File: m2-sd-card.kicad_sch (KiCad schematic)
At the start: 16 parts, among them J101 M.2_Key_E, J102 Conn_01x02, J103 Conn_02x03_Counter_Clockwise, J104 Conn_02x03_Counter_Clockwise, J105 Conn_01x01, J106 Conn_01x03, J107 Conn_01x02, J108 USB_B_Micro, J109 Micro_SD, U101 SN74LV1T34DBV

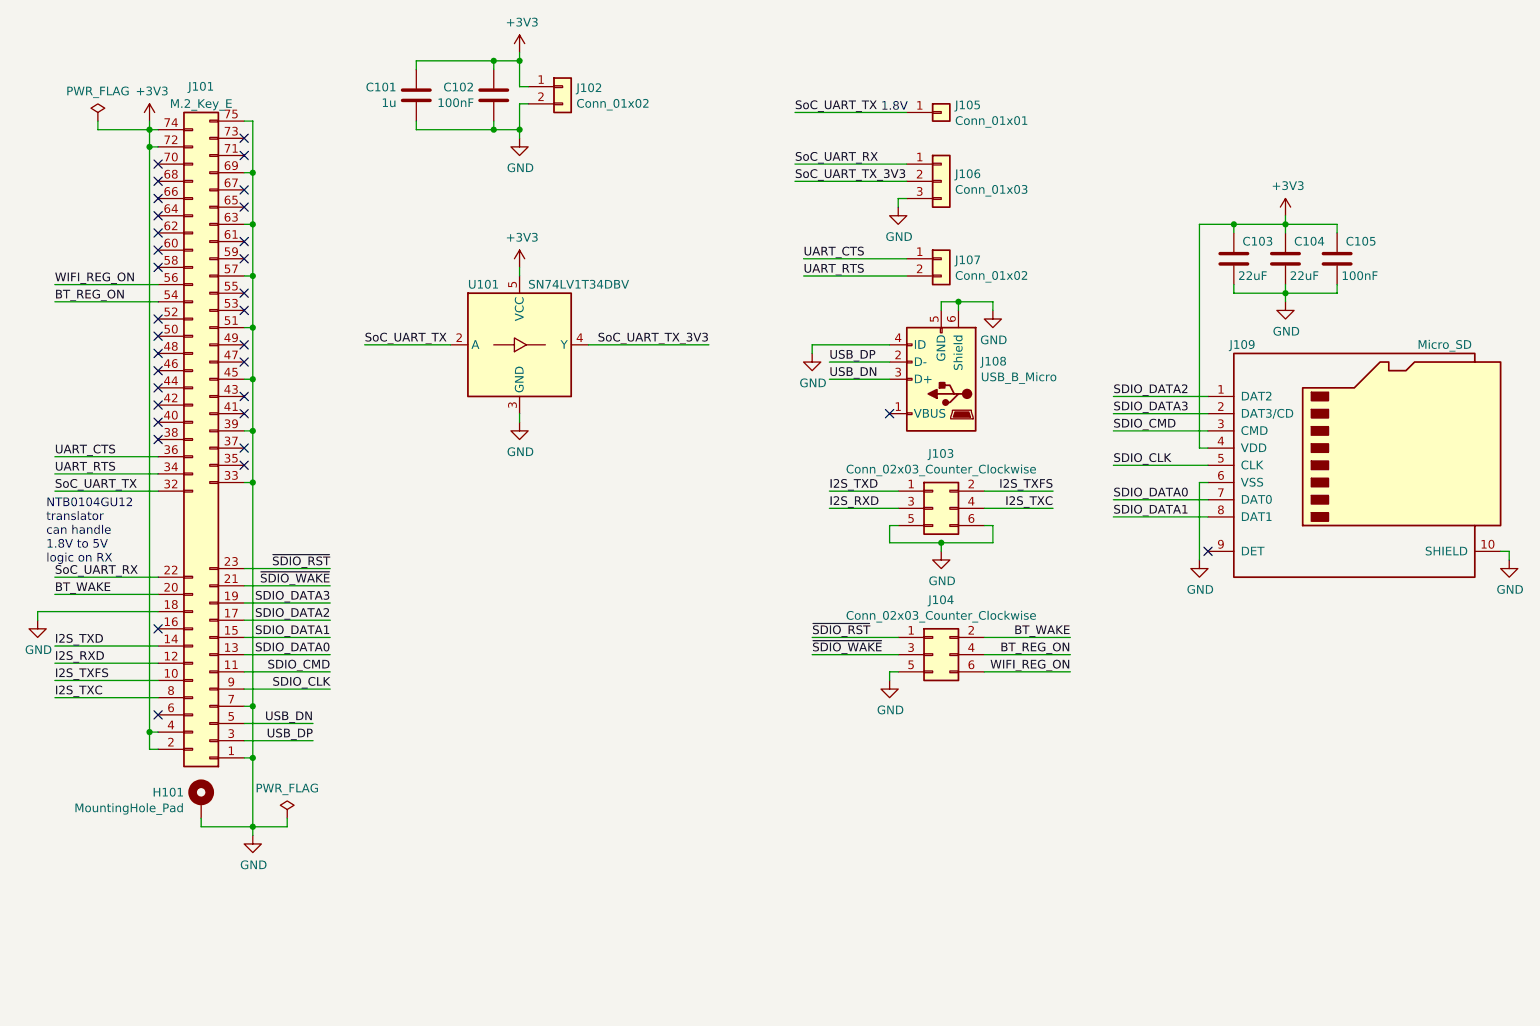
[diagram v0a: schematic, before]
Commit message: Update the schematic to use the NVT4857UK SD 3.0-compliant bidirectional level translator
Use Hirose DM3AT-SF-PEJM5 for the MicroSD card slot/connector (using
KiCad's built-in library, with the footprint backed up in the project
library).

Add a AP2120N-1.8 1.8V LDO to supply NVT4857UK's VCCA.

Create the NVT4857UK schematic symbol and footprint.

Create the AP2120N-18 schematic symbol.

Connect everything in the schematic, annotate all parts, and make sure
ERC passes.

Capacitors' and resistors' part numbers still need to be selected and
their attributes updated accordingly. Then the netlist can be imported
into the layout and the BOM exported.

At least 4mil trace width/space is likely needed due to the WLCSP-20
BGA package.
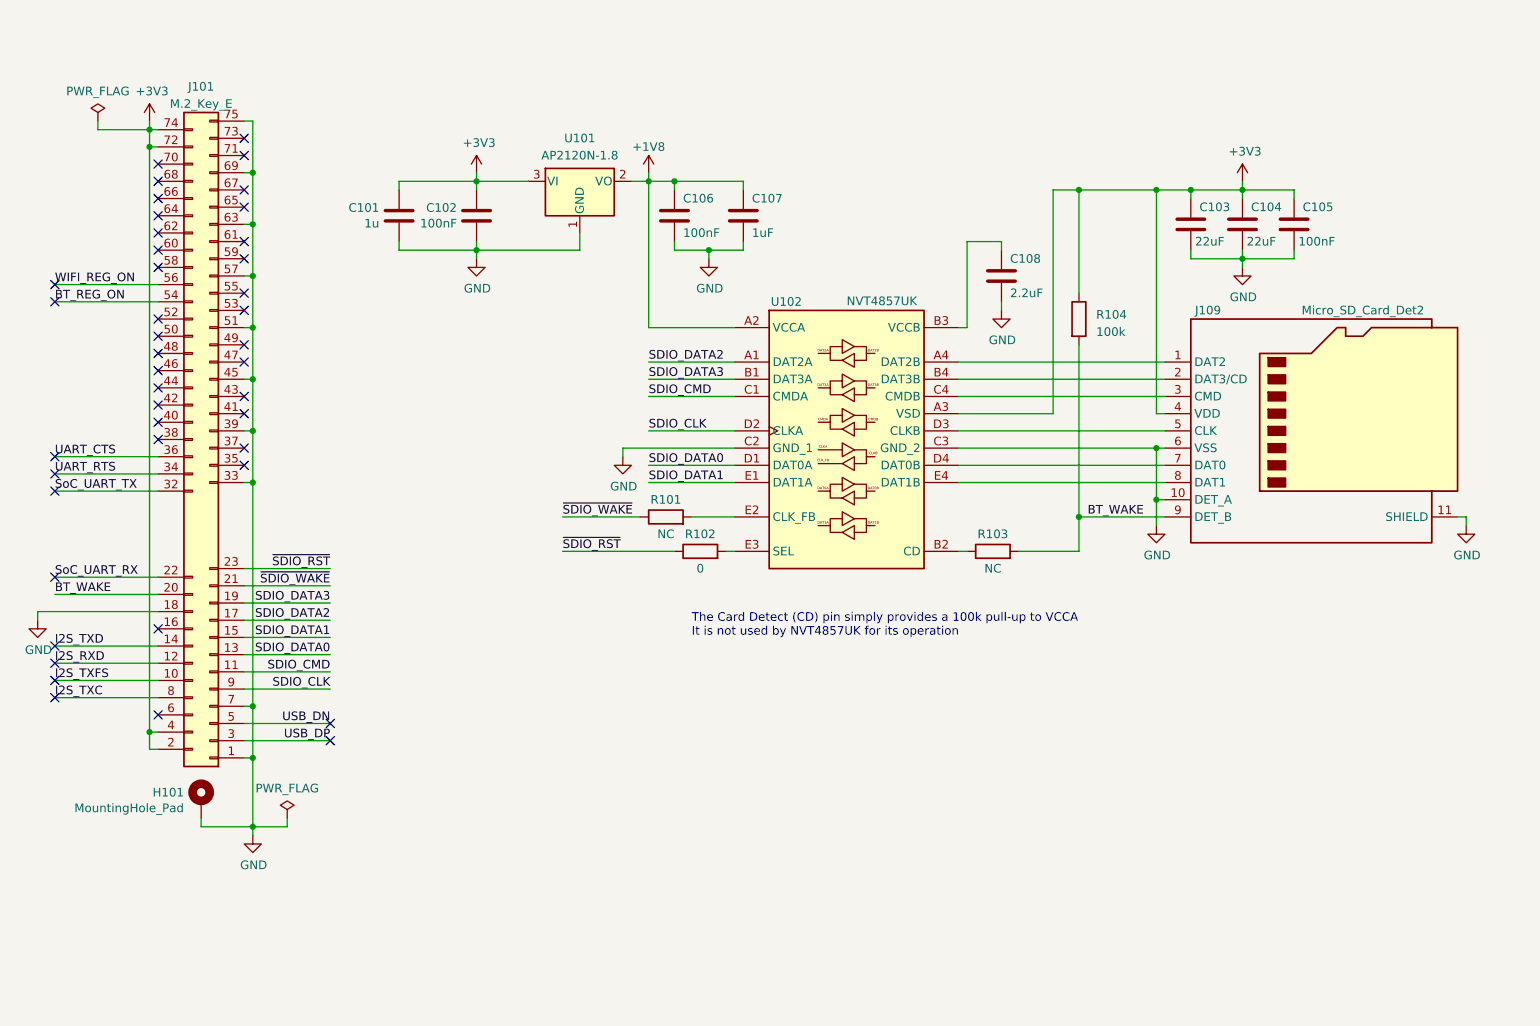
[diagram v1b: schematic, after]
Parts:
- removed J102: Conn_01x02, Connector_PinHeader_2.54mm:PinHeader_1x02_P2.54mm_Vertical, symbol Connector_Generic:Conn_01x02
- removed J103, J104: Conn_02x03_Counter_Clockwise, Connector_PinHeader_1.27mm:PinHeader_2x03_P1.27mm_Vertical_SMD, symbol Connector_Generic:Conn_02x03_Odd_Even
- removed J105: Conn_01x01, Connector_PinHeader_2.54mm:PinHeader_1x01_P2.54mm_Vertical, symbol Connector_Generic:Conn_01x01
- removed J106: Conn_01x03, Connector_PinHeader_2.54mm:PinHeader_1x03_P2.54mm_Vertical, symbol Connector_Generic:Conn_01x03
- removed J107: Conn_01x02, Connector_PinHeader_1.27mm:PinHeader_1x02_P1.27mm_Vertical_SMD_Pin1Right, symbol Connector_Generic:Conn_01x02
- removed J108: USB_B_Micro, Connector_USB:USB_Micro-B_Wuerth_614105150721_Vertical, symbol Connector:USB_OTG
- removed J109: Micro_SD, m2-sd-card:ALPS_SCHA4B0419, symbol m2-sd-card:Micro_SD_Card_Det_ALPS_SCHA
- removed U101: SN74LV1T34DBV, Package_TO_SOT_SMD:SOT-23-5_HandSoldering, symbol m2-sd-card:SN74LV1T34DBV
- added C106: 100nF, Capacitor_SMD:C_0402_1005Metric, symbol Device:C
- added C107: 1uF, Capacitor_SMD:C_0402_1005Metric, symbol Device:C
- added C108: 2.2uF, Capacitor_SMD:C_0402_1005Metric, symbol Device:C
- added J109: Micro_SD_Card_Det2, Connector_Card:microSD_HC_Hirose_DM3AT-SF-PEJM5, symbol Connector:Micro_SD_Card_Det2
- added R101, R103: NC, Resistor_SMD:R_0402_1005Metric, symbol Device:R
- added R102: 0, Resistor_SMD:R_0402_1005Metric, symbol Device:R
- added R104: 100k, Resistor_SMD:R_0402_1005Metric, symbol Device:R
- added U101: AP2120N-1.8, Package_TO_SOT_SMD:SOT-23, symbol m2-sd-card:AP2120N-1.8
- added U102: NVT4857UK, m2-sd-card:NVT4857UK, symbol m2-sd-card:NVT4857UK
- C101, C102, C103, C104, C105: footprint Capacitor_SMD:C_0603_1608Metric_Pad1.05x0.95mm_HandSolder -> Capacitor_SMD:C_0402_1005Metric
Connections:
- net +3V3: now also J109.4 (VDD), R104.1, U101.3 (VI), U102.A3 (VSD)
- net BT_WAKE: now also J109.9 (DET_B), R103.2, R104.2
- net GND: now also C106.2, C107.2, C108.2, J109.10 (DET_A), J109.11 (SHIELD), J109.6 (VSS), U101.1 (GND), U102.C2 (GND_1), U102.C3 (GND_2)
- net SDIO_CLK: now also U102.D2 (CLKA)
- net SDIO_CMD: now also U102.C1 (CMDA)
- net SDIO_DATA0: now also U102.D1 (DAT0A)
- net SDIO_DATA1: now also U102.E1 (DAT1A)
- net SDIO_DATA2: now also U102.A1 (DAT2A)
- net SDIO_DATA3: now also U102.B1 (DAT3A)
- net ~{SDIO_RST}: now also R102.1
- net ~{SDIO_WAKE}: now also R101.1
- new net: R102.2, U102.E3 (SEL)
- new net: C108.1, U102.B3 (VCCB)
- new net: J109.1 (DAT2), U102.A4 (DAT2B)
- new net: R103.1, U102.B2 (CD)
- new net: J109.2 (DAT3/CD), U102.B4 (DAT3B)
- new net: J109.3 (CMD), U102.C4 (CMDB)
- new net: J109.5 (CLK), U102.D3 (CLKB)
- new net: J109.7 (DAT0), U102.D4 (DAT0B)
- new net: R101.2, U102.E2 (CLK_FB)
- new net: J109.8 (DAT1), U102.E4 (DAT1B)
- new net +1V8: C106.1, C107.1, U101.2 (VO), U102.A2 (VCCA)
- no-connect marks 33 -> 43
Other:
- note added: "The Card Detect (CD) pin simply provides a 100k pull-up to VCCA It is not used by NVT4857UK for its operation"
- note removed: "1.8V"
- note removed: "NTB0104GU12 translator can handle 1.8V to 5V logic on RX"
- moved on the sheet: C101, C102, C103, C104, C105

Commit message: Fill out the remaining attributes for the passives and export the BOM and schematic as a PDF
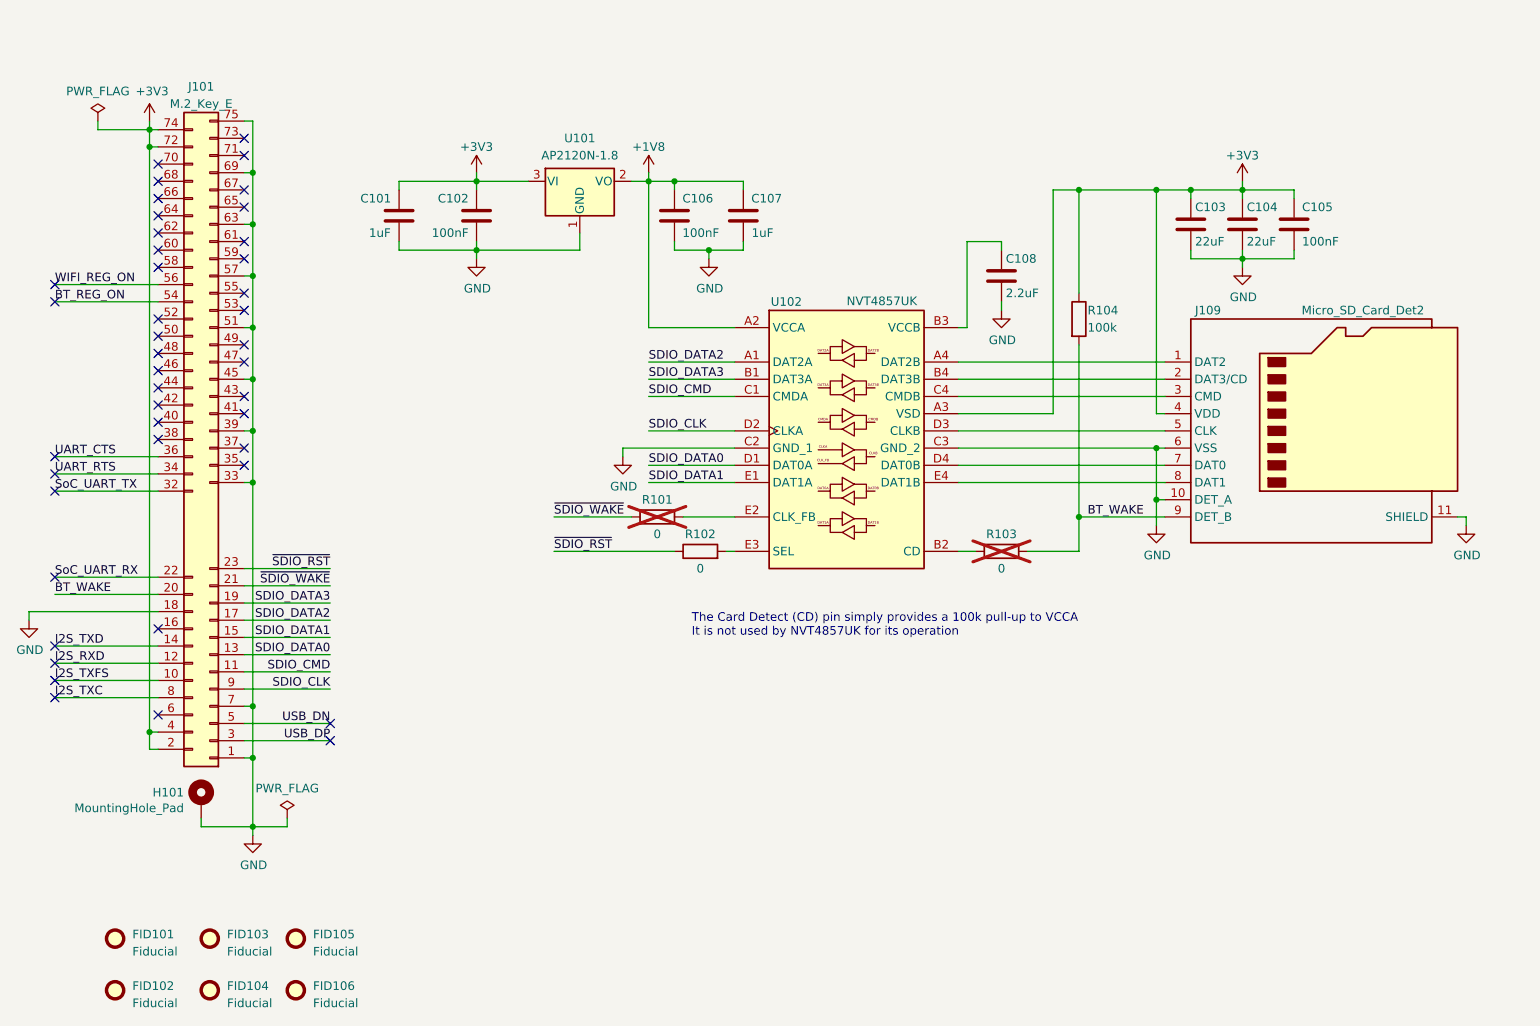
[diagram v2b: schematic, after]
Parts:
- added FID101, FID102, FID103, FID104, FID105, FID106: Fiducial, Fiducial:Fiducial_0.5mm_Mask1mm, symbol Mechanical:Fiducial
- C101: value 1u -> 1uF; Distrib Link (none) -> https://www.mouser.com/ProductDetail/Samsung-Electro-Mechan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; Distrib PN (none) -> 187-CL05A105KO5NNNC; MFG Name (none) -> Samsung; MFG Part Num (none) -> CL05A105KO5NNNC; Others (none) -> https://www.mouser.com/c/passive-components/capacitors/mlcc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; Tolerance (none) -> 10%
- C102, C105, C106: Distrib Link (none) -> https://www.mouser.com/ProductDetail/Samsung-Electro-Mechan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; Distrib PN (none) -> 187-CL05A104KA5NNNC; MFG Name (none) -> Samsung; MFG Part Num (none) -> CL05A104KA5NNNC; Others (none) -> https://www.mouser.com/c/passive-components/capacitors/mlcc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; Tolerance (none) -> 10%
- C103, C104: Distrib Link (none) -> https://www.mouser.com/ProductDetail/KYOCERA-AVX/CM05X5R226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; Distrib PN (none) -> 346-CM05X5R226M6AH80; MFG Name (none) -> KYOCERA AVX; MFG Part Num (none) -> CM05X5R226M06AH080; Others (none) -> https://www.digikey.com/en/products/detail/kyocera-avx/CM05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; Tolerance (none) -> 20%
- C107: Distrib Link (none) -> https://www.mouser.com/ProductDetail/Samsung-Electro-Mechan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; Distrib PN (none) -> 187-CL05A105KO5NNNC; MFG Name (none) -> Samsung; MFG Part Num (none) -> CL05A105KO5NNNC; Others (none) -> https://www.mouser.com/c/passive-components/capacitors/mlcc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; Tolerance (none) -> 10%
- C108: Distrib Link (none) -> https://www.mouser.com/ProductDetail/Samsung-Electro-Mechan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; Distrib PN (none) -> 187-CL05A225MQ5NNNC; MFG Name (none) -> Samsung; MFG Part Num (none) -> CL05A225MQ5NNNC; Others (none) -> https://www.mouser.com/c/passive-components/capacitors/mlcc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; Tolerance (none) -> 20%
- R101, R103: value NC -> 0; Distrib Link (none) -> https://www.mouser.com/ProductDetail/Vishay-Dale/CRCW040200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; Distrib PN (none) -> 71-CRCW04020000Z0EDC; MFG Name (none) -> Vishay; MFG Part Num (none) -> CRCW04020000Z0EDC; Others (none) -> https://www.mouser.com/c/passive-components/resistors/smd-r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; Tolerance (none) -> -; now not fitted
- R102: Distrib Link (none) -> https://www.mouser.com/ProductDetail/Vishay-Dale/CRCW040200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; Distrib PN (none) -> 71-CRCW04020000Z0EDC; MFG Name (none) -> Vishay; MFG Part Num (none) -> CRCW04020000Z0EDC; Others (none) -> https://www.mouser.com/c/passive-components/resistors/smd-r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; Tolerance (none) -> -
- R104: Distrib Link (none) -> https://www.mouser.com/ProductDetail/Panasonic/ERJ-2RKF1003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; Distrib PN (none) -> 667-ERJ-2RKF1003X; MFG Name (none) -> Panasonic; MFG Part Num (none) -> ERJ-2RKF1003X; Others (none) -> https://www.mouser.com/ProductDetail/Walsin/WR04X1003FTL?qs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; Tolerance (none) -> 1%
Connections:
- net +3V3: now also C101.1, C102.1, C103.1, C104.1, C105.1; no longer C101.2, C102.2, C103.2, C104.2, C105.2
- net GND: now also C101.2, C102.2, C103.2, C104.2, C105.2; no longer C101.1, C102.1, C103.1, C104.1, C105.1
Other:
- moved on the sheet: C103

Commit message: Hook up all of the nets and make sure DRC is passing
Exceptions were made for the half-mounting hole and a silkscreen overlap
with C3.

Reset the reference designators to first free number starting at 0 so
that they take up less space on the silkscreen.

Layout is not completely done and still needs to be polished up.
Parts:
- removed FID104, FID105, FID106: Fiducial, Fiducial:Fiducial_0.5mm_Mask1mm, symbol Mechanical:Fiducial
- renumbered C101 to C1, C102 to C2, C106 to C3, C107 to C4, C108 to C5, C103 to C6, C104 to C7, C105 to C8, FID101 to FID1, FID102 to FID2, FID103 to FID3, H101 to H1, J101 to J1, J109 to J2, R101 to R1, R102 to R2, R103 to R3, R104 to R4, U101 to U1, U102 to U2
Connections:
- net ~{SDIO_RST}: now also R1.1; no longer R2.1
- net ~{SDIO_WAKE}: now also R2.1; no longer R1.1
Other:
- moved on the sheet: FID1, FID2, FID3
